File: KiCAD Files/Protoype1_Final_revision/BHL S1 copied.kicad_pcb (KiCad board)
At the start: 4 copper layers, 70 x 70 mm, 93 parts, among them IC1 NUP2105LT1G, IC2 NUP2105LT1G, IC4 FD6288Q, J1 39-30-1042, J2 Conn_01x03_Pin, J3 Conn_01x03_Pin, J4 39-30-1042, Q1 CSD19502Q5B, Q2 CSD19502Q5B, Q3 CSD19502Q5B, Q4 CSD19502Q5B, Q5 CSD19502Q5B, Q7 CSD19502Q5B, SW1 PTS636 SM50J SMTR LFS, U1 ME6211C30M5, U2 SPX3819M5-L-5-0, U3 Solder Pad, U5 STM32G431CBU6, Y1 8MHz

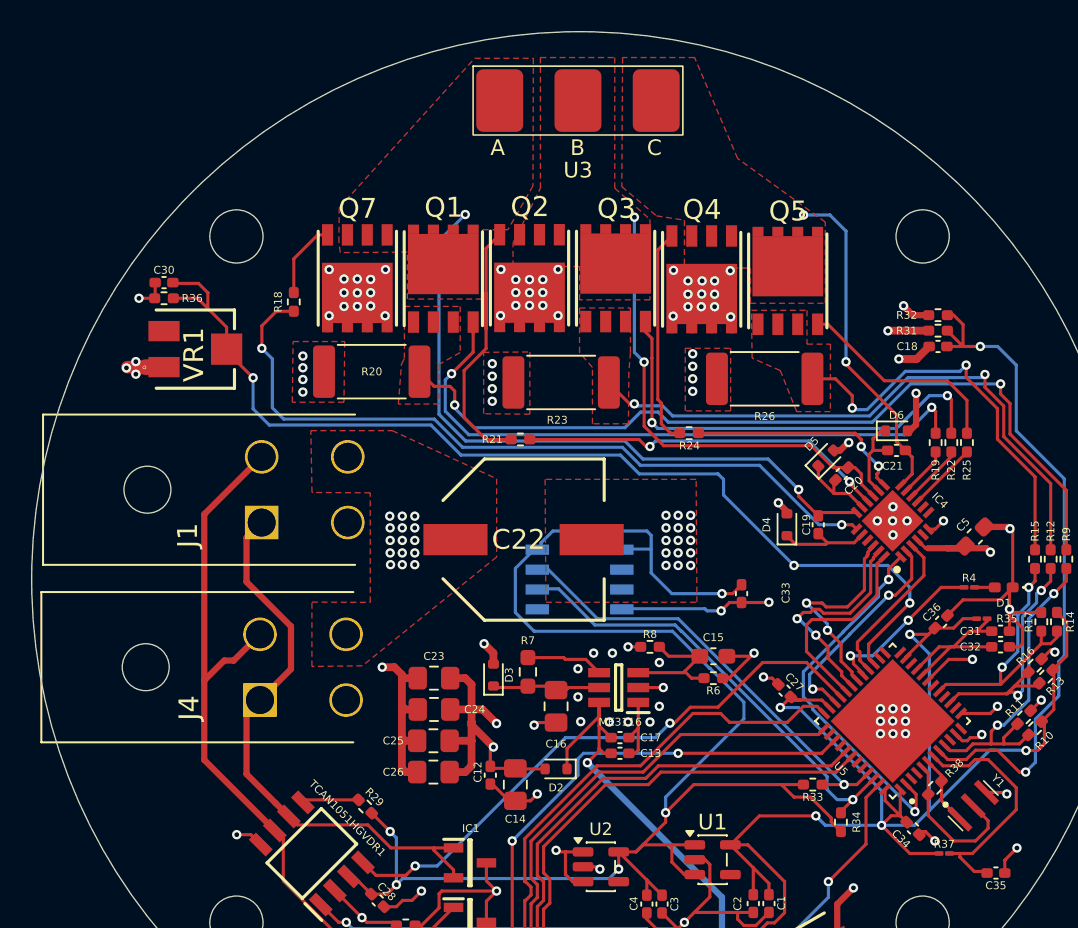
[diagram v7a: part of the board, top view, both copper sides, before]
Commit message: Fixed some traces.
This is the final revision before sending to manufacture
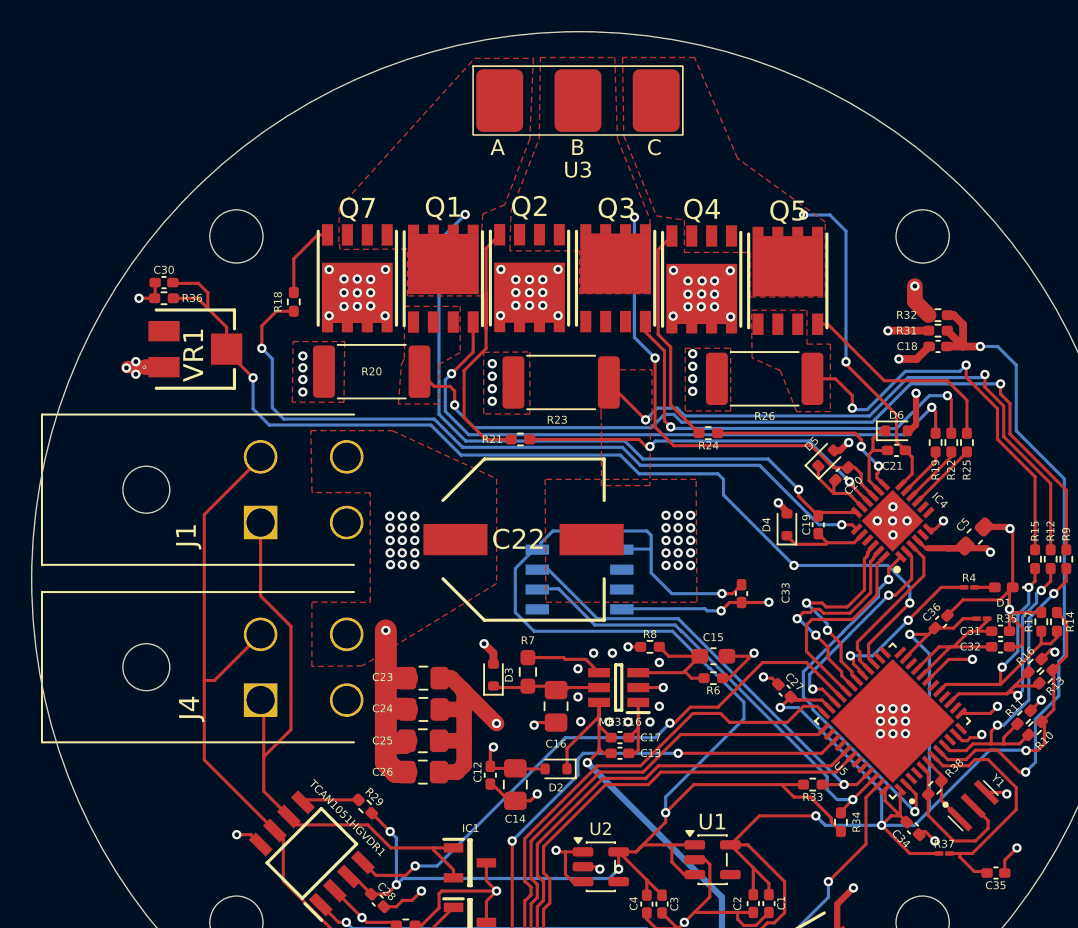
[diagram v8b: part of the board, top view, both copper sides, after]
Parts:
- moved R24 1.22 mm to (150.6, 86.0)
- moved C23 0.68 mm to (132.4, 101.7)
- moved C24 0.68 mm to (132.4, 103.7)
- moved C25 0.68 mm to (132.4, 105.7)
- moved C26 0.68 mm to (132.4, 107.7)
- moved J1 0.07 mm to (122.0, 91.7)
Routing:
- net DCBUS: track 33.4 -> 35.8 mm
- net CAN_L: track 36.4 -> 38.5 mm
- net GH_C: track 14.2 -> 12.9 mm
- net Vshunt_2+: track 38.4 -> 39.0 mm
- net Net-(Q3-G): track 29.0 -> 28.5 mm
